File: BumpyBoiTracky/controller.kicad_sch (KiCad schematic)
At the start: 4 parts

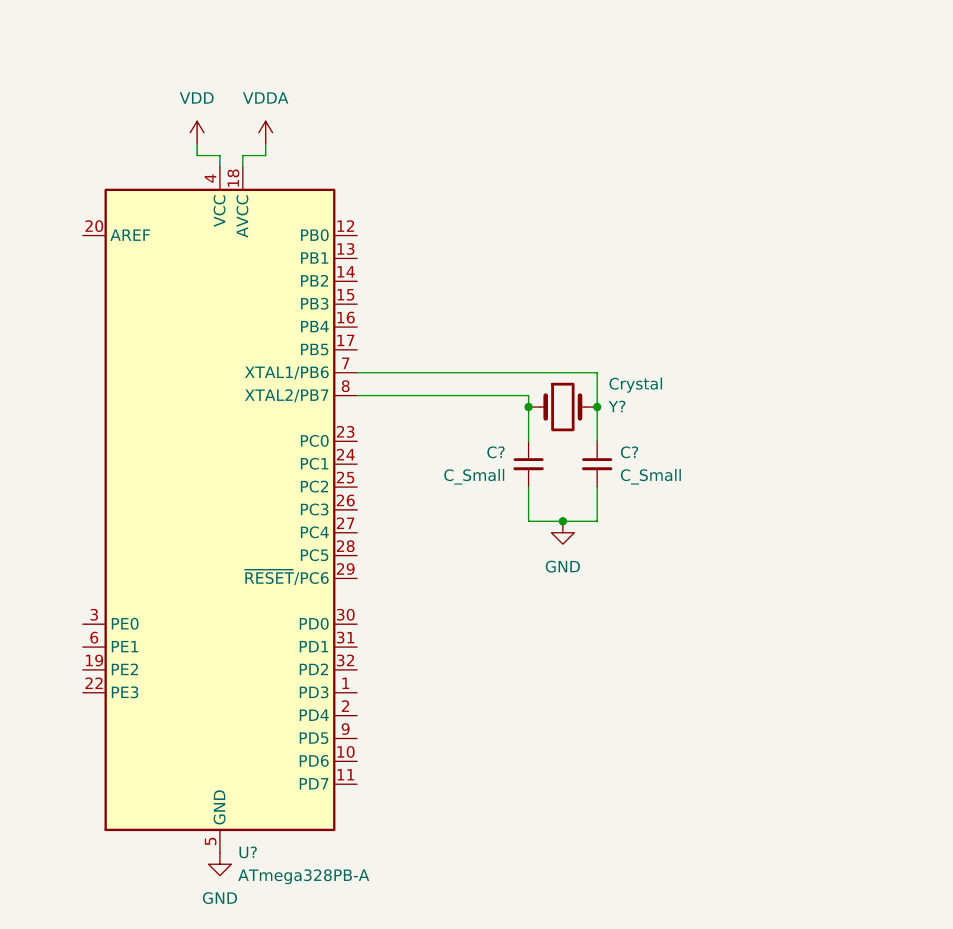
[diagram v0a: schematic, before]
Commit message: Controller Added
Added controller and Sensor. Begun work on prog interface
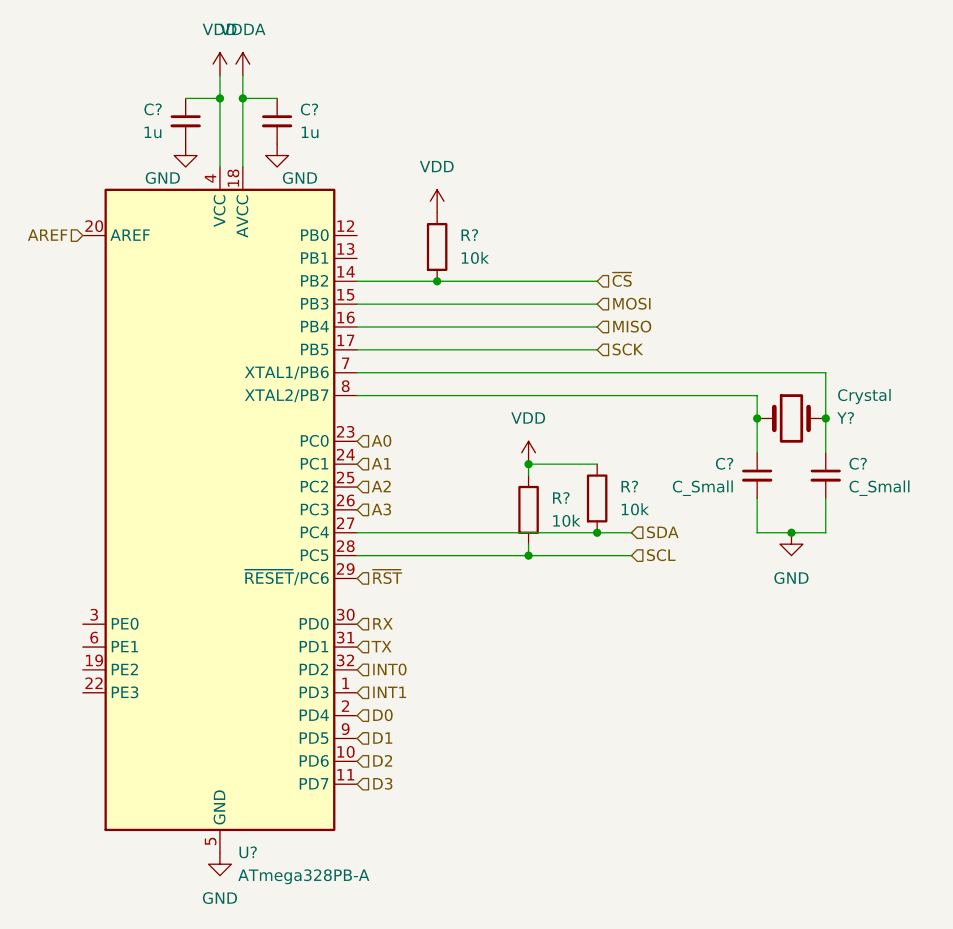
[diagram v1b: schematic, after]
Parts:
- added C? (x2): 1u, symbol Device:C_Small
- added R? (x3): 10k, symbol Device:R
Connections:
- net GND: now also C?.2, C?.2
- net VDD: now also C?.1, R?.1, R?.1, R?.1
- net VDDA: now also C?.1
- net INT1: now reaches U?.1 (PD3)
- net D2: now reaches U?.10 (PD6)
- net D3: now reaches U?.11 (PD7)
- net ~{CS}: now reaches U?.14 (PB2)
- net ~{CS}: now also R?.2
- net MOSI: now reaches U?.15 (PB3)
- net MISO: now reaches U?.16 (PB4)
- net SCK: now reaches U?.17 (PB5)
- net D0: now reaches U?.2 (PD4)
- net AREF: now reaches U?.20 (AREF)
- net A0: now reaches U?.23 (PC0)
- net A1: now reaches U?.24 (PC1)
- net A2: now reaches U?.25 (PC2)
- net A3: now reaches U?.26 (PC3)
- net SDA: now reaches U?.27 (PC4)
- net SDA: now also R?.2
- net SCL: now reaches U?.28 (PC5)
- net SCL: now also R?.2
- net ~{RST}: now reaches U?.29 (~{RESET}/PC6)
- net RX: now reaches U?.30 (PD0)
- net TX: now reaches U?.31 (PD1)
- net INT0: now reaches U?.32 (PD2)
- net D1: now reaches U?.9 (PD5)
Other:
- moved on the sheet: C?, Y?

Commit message: (adding forgotten files)
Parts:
- removed C? (x2): C_Small, symbol Device:C_Small
- removed Y?: Crystal, symbol Device:Crystal
- added C3, C4: 20p, Capacitor_SMD:C_0603_1608Metric, symbol Device:C_Small
- added J4, J5, J6, J7: Conn_01x08_Female, Connector_PinHeader_2.54mm:PinHeader_1x08_P2.54mm_Vertical, symbol Connector:Conn_01x08_Female
- added J8: ICSP, Connector_PinHeader_2.54mm:PinHeader_2x03_P2.54mm_Vertical, symbol Connector_Generic:Conn_02x03_Counter_Clockwise
- added JP1, JP10, JP11, JP12, JP13, JP14, JP15, JP16, JP17, JP18, JP19, JP2, JP20, JP21, JP22, JP23, JP24, JP25, JP26, JP27, JP28, JP3, JP4, JP5, JP8, JP9: SolderJumper_2_Bridged, Jumper:SolderJumper-2_P1.3mm_Bridged_RoundedPad1.0x1.5mm, symbol Jumper:SolderJumper_2_Bridged
- added JP6, JP7: SolderJumper_2_Open, Jumper:SolderJumper-2_P1.3mm_Open_RoundedPad1.0x1.5mm, symbol Jumper:SolderJumper_2_Open
- added Y1: 8MHz, Crystal:Crystal_SMD_HC49-SD, symbol Device:Crystal_Small
- C1, C2: renamed from C?; footprint (none) -> Capacitor_SMD:C_0603_1608Metric
- R6, R7, R8: renamed from R?; footprint (none) -> Resistor_SMD:R_0603_1608Metric
- gave numbers to parts that had none: 1
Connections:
- net A0: now also JP16.2 (B); no longer U1.23 (PC0)
- net A1: now also JP10.2 (B); no longer U1.24 (PC1)
- net A2: now also JP13.2 (B); no longer U1.25 (PC2)
- net A3: now also JP17.2 (B); no longer U1.26 (PC3)
- net AREF: now also JP5.1 (A); no longer U1.20 (AREF)
- net D0: now also JP19.2 (B); no longer U1.2 (PD4)
- net D1: now also JP28.2 (B); no longer U1.9 (PD5)
- net D2: now also JP24.2 (B); no longer U1.10 (PD6)
- net D3: now also JP20.2 (B); no longer U1.11 (PD7)
- net GND: now also C3.2, C4.2, J4.5 (Pin_5), J6.5 (Pin_5), J8.4 (Pin_4)
- net INT0: now also JP27.2 (B); no longer U1.32 (PD2)
- net INT1: now also JP23.2 (B); no longer U1.1 (PD3)
- net MISO: now also JP12.2 (B); no longer U1.16 (PB4)
- net MOSI: now also JP15.2 (B); no longer U1.15 (PB3)
- net RX: now also JP22.2 (B); no longer U1.30 (PD0)
- net SCK: now also JP9.2 (B); no longer U1.17 (PB5)
- net SCL: now also JP21.2 (B); no longer R6.2, U1.28 (PC5)
- net SDA: now also JP25.2 (B); no longer R8.2, U1.27 (PC4)
- net TX: now also JP18.2 (B); no longer U1.31 (PD1)
- net VDD: now also J4.4 (Pin_4), J8.6 (Pin_6), JP6.2 (B); no longer C1.1, U1.4 (VCC)
- net VDDA: now also J6.2 (Pin_2), JP7.2 (B); no longer C2.1, U1.18 (AVCC)
- net ~{CS}: now also JP8.2 (B); no longer U1.14 (PB2)
- net ~{RST}: now also JP26.2 (B); no longer U1.29 (~{RESET}/PC6)
- net at U1.8 (XTAL2/PB7): now also C3.1, J4.8 (Pin_8), Y1.1
- net at U1.7 (XTAL1/PB6): now also C4.1, J4.7 (Pin_7), Y1.2
- net at U1.12 (PB0): now also J5.4 (Pin_4), JP14.1 (A)
- net at U1.13 (PB1): now also J5.5 (Pin_5), JP11.1 (A)
- net at U1.19 (PE2): now also J6.3 (Pin_3), JP2.2 (B)
- net at U1.22 (PE3): now also J6.6 (Pin_6), JP4.2 (B)
- net at U1.3 (PE0): now also J4.3 (Pin_3), JP3.2 (B)
- net at U1.6 (PE1): now also J4.6 (Pin_6), JP1.2 (B)
- new net: J7.7 (Pin_7), JP18.1 (A), U1.31 (PD1)
- new net: C1.1, JP6.1 (A), U1.4 (VCC)
- new net: J7.5 (Pin_5), J8.3 (Pin_3), JP26.1 (A), U1.29 (~{RESET}/PC6)
- new net: J6.1 (Pin_1), J8.2 (Pin_2), JP9.1 (A), U1.17 (PB5)
- new net: J5.8 (Pin_8), J8.1 (Pin_1), JP12.1 (A), U1.16 (PB4)
- new net: J5.7 (Pin_7), J8.5 (Pin_5), JP15.1 (A), U1.15 (PB3)
- new net: J7.1 (Pin_1), JP13.1 (A), U1.25 (PC2)
- new net: J7.2 (Pin_2), JP17.1 (A), U1.26 (PC3)
- new net: J7.3 (Pin_3), JP25.1 (A), R8.2, U1.27 (PC4)
- new net: J7.4 (Pin_4), JP21.1 (A), R6.2, U1.28 (PC5)
- new net: J7.6 (Pin_6), JP22.1 (A), U1.30 (PD0)
- new net: J7.8 (Pin_8), JP27.1 (A), U1.32 (PD2)
- new net: J6.4 (Pin_4), JP5.2 (B), U1.20 (AREF)
- new net: J6.7 (Pin_7), JP16.1 (A), U1.23 (PC0)
- new net: J5.1 (Pin_1), JP28.1 (A), U1.9 (PD5)
- new net: J5.2 (Pin_2), JP24.1 (A), U1.10 (PD6)
- new net: J5.3 (Pin_3), JP20.1 (A), U1.11 (PD7)
- new net: J5.6 (Pin_6), JP8.1 (A), U1.14 (PB2)
- new net: C2.1, JP7.1 (A), U1.18 (AVCC)
- new net: J4.1 (Pin_1), JP23.1 (A), U1.1 (PD3)
- new net: J4.2 (Pin_2), JP19.1 (A), U1.2 (PD4)
- new net: J6.8 (Pin_8), JP10.1 (A), U1.24 (PC1)
- new net PB0: JP14.2 (B)
- new net PB1: JP11.2 (B)
- new net PE0: JP3.1 (A)
- new net PE1: JP1.1 (A)
- new net PE2: JP2.1 (A)
- new net PE3: JP4.1 (A)
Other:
- note added: "Breakout Hell"
- note added: "ICSP Header"
- moved on the sheet: C1, C2, R6, R7, R8, U1

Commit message: Began layout for circuit board
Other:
- moved on the sheet: JP1, JP2, JP3, JP4
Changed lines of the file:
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@@
     (stroke (width 0) (type default) (color 0 0 0 0))
   )
-  (wire (pts (xy 52.07 104.14) (xy 73.66 104.14))
+  (wire (pts (xy 52.07 104.14) (xy 72.39 104.14))
     (stroke (width 0) (type default) (color 0 0 0 0))
   )
@@
     (stroke (width 0) (type default) (color 0 0 0 0))
   )
-  (wire (pts (xy 72.39 101.6) (xy 87.63 101.6))
+  (wire (pts (xy 71.12 101.6) (xy 87.63 101.6))
     (stroke (width 0) (type default) (color 0 0 0 0))
   )
@@
     (stroke (width 0) (type default) (color 0 0 0 0))
   )
-  (wire (pts (xy 52.07 96.52) (xy 73.66 96.52))
+  (wire (pts (xy 52.07 96.52) (xy 72.39 96.52))
     (stroke (width 0) (type default) (color 0 0 0 0))
   )
@@
     (stroke (width 0) (type default) (color 0 0 0 0))
   )
-  (wire (pts (xy 81.28 96.52) (xy 82.55 96.52))
+  (wire (pts (xy 80.01 96.52) (xy 82.55 96.52))
     (stroke (width 0) (type default) (color 0 0 0 0))
   )
@@
     (stroke (width 0) (type default) (color 0 0 0 0))
   )
-  (wire (pts (xy 52.07 101.6) (xy 64.77 101.6))
+  (wire (pts (xy 52.07 101.6) (xy 63.5 101.6))
     (stroke (width 0) (type default) (color 0 0 0 0))
   )
@@
     (stroke (width 0) (type default) (color 0 0 0 0))
   )
-  (wire (pts (xy 81.28 104.14) (xy 92.71 104.14))
+  (wire (pts (xy 80.01 104.14) (xy 92.71 104.14))
     (stroke (width 0) (type default) (color 0 0 0 0))
   )
@@
     (stroke (width 0) (type default) (color 0 0 0 0))
   )
-  (wire (pts (xy 52.07 99.06) (xy 54.61 99.06))
+  (wire (pts (xy 52.07 99.06) (xy 53.34 99.06))
     (stroke (width 0) (type default) (color 0 0 0 0))
   )
@@
     (stroke (width 0) (type default) (color 0 0 0 0))
   )
-  (wire (pts (xy 62.23 99.06) (xy 85.09 99.06))
+  (wire (pts (xy 60.96 99.06) (xy 85.09 99.06))
     (stroke (width 0) (type default) (color 0 0 0 0))
   )
@@
     (pin "2")
   )
-  (symbol (lib_id "Jumper:SolderJumper_2_Bridged") (at 77.47 96.52 0) (unit 1)
-    (in_bom yes) (on_board yes) (fields_autoplaced)
-    (property "Reference" "JP3" (id 0) (at 77.47 92.71 0))
-    (property "Value" "SolderJumper_2_Bridged" (id 1) (at 77.47 92.71 0)
-      (effects (font (size 1.27 1.27)) hide)
-    )
-    (property "Footprint" "Jumper:SolderJumper-2_P1.3mm_Bridged_RoundedPad1.0x1.5mm" (id 2) (at 77.47 96.52 0)
-      (effects (font (size 1.27 1.27)) hide)
-    )
-    (property "Datasheet" "~" (id 3) (at 77.47 96.52 0)
+  (symbol (lib_id "Jumper:SolderJumper_2_Bridged") (at 76.2 96.52 0) (unit 1)
+    (in_bom yes) (on_board yes) (fields_autoplaced)
+    (property "Reference" "JP3" (id 0) (at 76.2 92.71 0))
+    (property "Value" "SolderJumper_2_Bridged" (id 1) (at 76.2 92.71 0)
+      (effects (font (size 1.27 1.27)) hide)
+    )
+    (property "Footprint" "Jumper:SolderJumper-2_P1.3mm_Bridged_RoundedPad1.0x1.5mm" (id 2) (at 76.2 96.52 0)
+      (effects (font (size 1.27 1.27)) hide)
+    )
+    (property "Datasheet" "~" (id 3) (at 76.2 96.52 0)
       (effects (font (size 1.27 1.27)) hide)
     )
@@
     (pin "2")
   )
-  (symbol (lib_id "Jumper:SolderJumper_2_Bridged") (at 68.58 101.6 0) (unit 1)
-    (in_bom yes) (on_board yes) (fields_autoplaced)
-    (property "Reference" "JP2" (id 0) (at 68.58 97.79 0))
-    (property "Value" "SolderJumper_2_Bridged" (id 1) (at 68.58 97.79 0)
-      (effects (font (size 1.27 1.27)) hide)
-    )
-    (property "Footprint" "Jumper:SolderJumper-2_P1.3mm_Bridged_RoundedPad1.0x1.5mm" (id 2) (at 68.58 101.6 0)
-      (effects (font (size 1.27 1.27)) hide)
-    )
-    (property "Datasheet" "~" (id 3) (at 68.58 101.6 0)
+  (symbol (lib_id "Jumper:SolderJumper_2_Bridged") (at 67.31 101.6 0) (unit 1)
+    (in_bom yes) (on_board yes) (fields_autoplaced)
+    (property "Reference" "JP2" (id 0) (at 67.31 97.79 0))
+    (property "Value" "SolderJumper_2_Bridged" (id 1) (at 67.31 97.79 0)
+      (effects (font (size 1.27 1.27)) hide)
+    )
+    (property "Footprint" "Jumper:SolderJumper-2_P1.3mm_Bridged_RoundedPad1.0x1.5mm" (id 2) (at 67.31 101.6 0)
+      (effects (font (size 1.27 1.27)) hide)
+    )
+    (property "Datasheet" "~" (id 3) (at 67.31 101.6 0)
       (effects (font (size 1.27 1.27)) hide)
     )
@@
     (pin "2")
   )
-  (symbol (lib_id "Jumper:SolderJumper_2_Bridged") (at 58.42 99.06 0) (unit 1)
-    (in_bom yes) (on_board yes) (fields_autoplaced)
-    (property "Reference" "JP1" (id 0) (at 58.42 95.25 0))
-    (property "Value" "SolderJumper_2_Bridged" (id 1) (at 58.42 95.25 0)
-      (effects (font (size 1.27 1.27)) hide)
-    )
-    (property "Footprint" "Jumper:SolderJumper-2_P1.3mm_Bridged_RoundedPad1.0x1.5mm" (id 2) (at 58.42 99.06 0)
-      (effects (font (size 1.27 1.27)) hide)
-    )
-    (property "Datasheet" "~" (id 3) (at 58.42 99.06 0)
-      (effects (font (size 1.27 1.27)) hide)
-    )
-    (pin "1")
-    (pin "2")
-  )
-  (symbol (lib_id "Jumper:SolderJumper_2_Bridged") (at 77.47 104.14 0) (unit 1)
-    (in_bom yes) (on_board yes) (fields_autoplaced)
-    (property "Reference" "JP4" (id 0) (at 77.47 100.33 0))
-    (property "Value" "SolderJumper_2_Bridged" (id 1) (at 77.47 100.33 0)
-      (effects (font (size 1.27 1.27)) hide)
-    )
-    (property "Footprint" "Jumper:SolderJumper-2_P1.3mm_Bridged_RoundedPad1.0x1.5mm" (id 2) (at 77.47 104.14 0)
-      (effects (font (size 1.27 1.27)) hide)
-    )
-    (property "Datasheet" "~" (id 3) (at 77.47 104.14 0)
-      (effects (font (size 1.27 1.27)) hide)
-    )
+  (symbol (lib_id "Jumper:SolderJumper_2_Bridged") (at 57.15 99.06 0) (unit 1)
+    (in_bom yes) (on_board yes) (fields_autoplaced)
+    (property "Reference" "JP1" (id 0) (at 57.15 95.25 0))
+    (property "Value" "SolderJumper_2_Bridged" (id 1) (at 57.15 95.25 0)
+      (effects (font (size 1.27 1.27)) hide)
+    )
+    (property "Footprint" "Jumper:SolderJumper-2_P1.3mm_Bridged_RoundedPad1.0x1.5mm" (id 2) (at 57.15 99.06 0)
+      (effects (font (size 1.27 1.27)) hide)
+    )
+    (property "Datasheet" "~" (id 3) (at 57.15 99.06 0)
+      (effects (font (size 1.27 1.27)) hide)
+    )
+    (pin "1")
+    (pin "2")
+  )
+  (symbol (lib_id "Jumper:SolderJumper_2_Bridged") (at 76.2 104.14 0) (unit 1)
+    (in_bom yes) (on_board yes) (fields_autoplaced)
+    (property "Reference" "JP4" (id 0) (at 76.2 100.33 0))
+    (property "Value" "SolderJumper_2_Bridged" (id 1) (at 76.2 100.33 0)
+      (effects (font (size 1.27 1.27)) hide)
+    )
+    (property "Footprint" "Jumper:SolderJumper-2_P1.3mm_Bridged_RoundedPad1.0x1.5mm" (id 2) (at 76.2 104.14 0)
+      (effects (font (size 1.27 1.27)) hide)
+    )
+    (property "Datasheet" "~" (id 3) (at 76.2 104.14 0)
+      (effects (font (size 1.27 1.27)) hide)
+    )
